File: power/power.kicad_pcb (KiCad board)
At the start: 4 copper layers, 75 x 56 mm, 66 parts, among them J1 GPIO, J10 SCL1, J11 SDA1, J12 SCL2, J13 SDA2, J14 VCC1, J15 GND1, J16 VCC2, J17 GND2, J18 JP_VCC_PWM, J19 Conn_01x01, J2 PWM_OUT, J3 PWM_IN, J4 JP_EXT, J5 JP_VOLTS, J6 I2C_EXT1, J7 I2C_EXT2, J8 PWM_OUT, J9 JP_VCC_PWM, Q1 D15P05, Q2 BC847C, U2 REF5050IDGK, U3 L78L06_SOT89, U5 TPS56A37RPAR

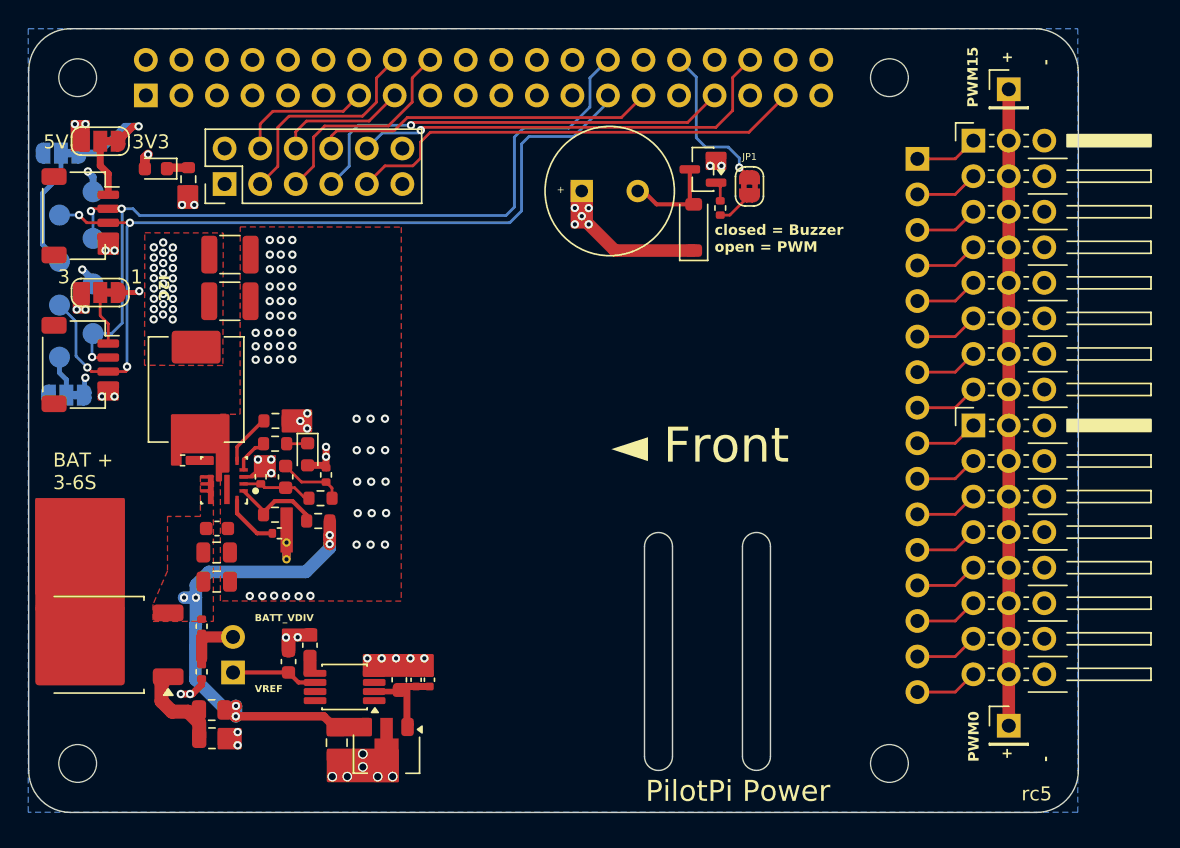
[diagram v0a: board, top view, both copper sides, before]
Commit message: cleanup vias & traces
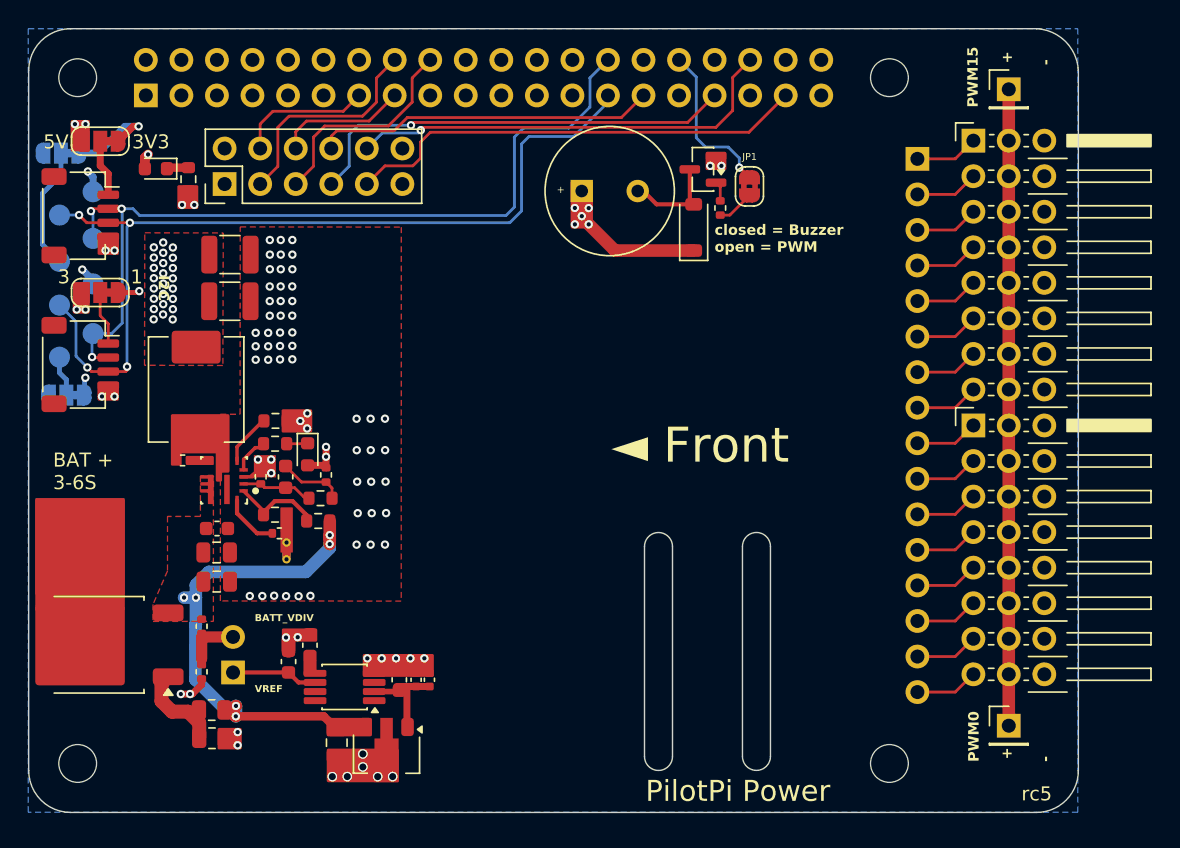
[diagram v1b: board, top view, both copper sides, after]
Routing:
- net +6V: track 7.85 -> 6.99 mm
- net /GPIO0/SDA0: track 65.6 -> 64.8 mm
- net +3V3: track 61.4 -> 60.7 mm
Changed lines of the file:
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@@
 			)
 		)
-		(attr through_hole exclude_from_pos_files dnp)
+		(attr through_hole exclude_from_pos_files)
 		(duplicate_pad_numbers_are_jumpers no)
 		(fp_line
@@
 			)
 		)
-		(attr through_hole exclude_from_pos_files dnp)
+		(attr through_hole exclude_from_pos_files)
 		(duplicate_pad_numbers_are_jumpers no)
 		(fp_line
@@
 			)
 		)
-		(attr through_hole exclude_from_bom dnp)
+		(attr through_hole exclude_from_bom)
 		(duplicate_pad_numbers_are_jumpers no)
 		(fp_line
@@
 			)
 		)
-		(attr through_hole exclude_from_bom dnp)
+		(attr through_hole exclude_from_bom)
 		(duplicate_pad_numbers_are_jumpers no)
 		(fp_line
@@
 			)
 		)
-		(property "Part" "2541WV-2X01P"
+		(property "Part" ""
 			(at 0 0 90)
 			(unlocked yes)
@@
 			)
 		)
-		(attr through_hole exclude_from_pos_files dnp)
+		(attr through_hole exclude_from_pos_files)
 		(duplicate_pad_numbers_are_jumpers no)
 		(fp_line
@@
 			)
 		)
-		(attr through_hole exclude_from_pos_files dnp)
+		(attr through_hole exclude_from_pos_files)
 		(duplicate_pad_numbers_are_jumpers no)
 		(fp_line
@@
 			)
 		)
-		(attr through_hole exclude_from_pos_files dnp)
+		(attr through_hole exclude_from_pos_files)
 		(duplicate_pad_numbers_are_jumpers no)
 		(fp_line
@@
 			)
 		)
-		(attr through_hole exclude_from_pos_files dnp)
+		(attr through_hole exclude_from_pos_files)
 		(duplicate_pad_numbers_are_jumpers no)
 		(fp_line
@@
 	)
 	(segment
-		(start 128.632625 91.000617)
-		(end 128.633153 91.000089)
-		(width 0.5)
-		(layer "F.Cu")
-		(net "+6V")
-	)
-	(segment
 		(start 126.401813 91.000617)
 		(end 126.402056 91.00086)
@@
 	)
 	(segment
-		(start 128.633153 91.000089)
-		(end 128.283153 91.000089)
-		(width 0.5)
-		(layer "F.Cu")
-		(net "+6V")
-	)
-	(segment
 		(start 127.026406 91.00086)
 		(end 127.026406 93.685086)
@@
 	)
 	(segment
-		(start 127.220881 93.740611)
-		(end 127.068469 93.893023)
-		(width 0.5)
-		(layer "F.Cu")
-		(net "+6V")
-	)
-	(segment
 		(start 126.279764 91.000617)
 		(end 126.279764 91.361598)
@@
 	)
 	(segment
-		(start 127.276406 93.685086)
-		(end 127.068469 93.893023)
-		(width 0.5)
-		(layer "F.Cu")
-		(net "+6V")
-	)
-	(segment
 		(start 127.279764 91.000617)
 		(end 128.632625 91.000617)
@@
 	)
 	(segment
-		(start 104.6 62.233333)
-		(end 104.6 61.98)
-		(width 0.5)
-		(layer "B.Cu")
-		(net "GND")
-	)
-	(segment
 		(start 104.6 61.98)
 		(end 103.83 61.21)
@@
 	)
 	(segment
-		(start 104.460176 62.373157)
-		(end 104.6 62.233333)
-		(width 0.5)
-		(layer "B.Cu")
-		(net "GND")
-	)
-	(segment
 		(start 120.461318 90.711598)
 		(end 119.280402 90.711598)
@@
 	)
 	(segment
-		(start 114.60414 89.99586)
-		(end 114.6 90)
-		(width 0.3)
-		(layer "F.Cu")
-		(net "/VREF")
-	)
-	(segment
-		(start 116.779441 78.728828)
-		(end 116.779441 78.561584)
-		(width 0.3)
-		(layer "F.Cu")
-		(net "Net-(U5-EN)")
-	)
-	(segment
 		(start 115.357178 77.033847)
 		(end 116.672159 78.348828)
@@
 	)
 	(segment
-		(start 118.347177 76.788846)
-		(end 118.357178 76.798847)
-		(width 0.2)
-		(layer "F.Cu")
-		(net "Net-(U5-FB)")
-	)
-	(segment
 		(start 116.846732 76.788846)
 		(end 118.347177 76.788846)
@@
 	)
 	(segment
-		(start 116.738413 72.022612)
-		(end 116.807178 72.022612)
-		(width 0.25)
-		(layer "F.Cu")
-		(net "Net-(U5-SS)")
-	)
-	(segment
 		(start 114.887179 73.873846)
 		(end 116.738413 72.022612)
@@
 	)
 	(segment
-		(start 104.53 65.853333)
-		(end 104.6 65.783333)
-		(width 0.2)
-		(layer "B.Cu")
-		(net "/GPIO1{slash}SCL0")
-	)
-	(segment
 		(start 106.64 56.864834)
 		(end 106.68 56.904834)
@@
 	)
 	(segment
-		(start 141.39 49.26)
-		(end 141.39 48.77)
-		(width 0.2)
-		(layer "B.Cu")
-		(net "/GPIO0{slash}SDA0")
-	)
-	(segment
 		(start 103.38 67.392159)
 		(end 103.38 64.93)
@@
 	)
 	(segment
-		(start 107.269888 57.864834)
-		(end 107.35 57.944946)
-		(width 0.2)
-		(layer "B.Cu")
-		(net "/GPIO0{slash}SDA0")
-	)
-	(segment
 		(start 104.191262 68.203421)
 		(end 103.38 67.392159)
@@
 	(segment
 		(start 107.23 57.864834)
-		(end 107.4 57.864834)
-		(width 0.2)
-		(layer "B.Cu")
-		(net "/GPIO0{slash}SDA0")
-	)
-	(segment
-		(start 107.23 57.864834)
 		(end 107.269888 57.864834)
 		(width 0.2)
@@
 	)
 	(segment
-		(start 108.37 48.77)
-		(end 107.855 49.285)
-		(width 0.35)
-		(layer "In1.Cu")
-		(net "+3V3")
-	)
-	(segment
 		(start 107.975 68.655)
 		(end 107.77 68.86)
@@
 	)
 	(segment
-		(start 114.596289 87.463711)
-		(end 114.6 87.46)
-		(width 0.8)
-		(layer "F.Cu")
-		(net "/BATT_VDIV")
-	)
-	(segment
 		(start 112.36 89.038711)
 		(end 112.36 87.463711)
@@
 	)
 	(segment
-		(start 147.24 56.275)
-		(end 147.515 56.55)
-		(width 0.3)
-		(layer "F.Cu")
-		(net "Net-(BZ1--)")
-	)
-	(segment
 		(start 147.515 56.55)
 		(end 144.865 56.55)
@@
 	)
 	(segment
-		(start 119.897178 73.653847)
-		(end 119.927178 73.623847)
-		(width 0.2)
-		(layer "F.Cu")
-		(net "Net-(D1-K)")
-	)
-	(segment
 		(start 150.775 53.93)
 		(end 150.814202 53.93)
@@
 	)
 	(segment
-		(start 150.615 53.77)
-		(end 150.775 53.93)
-		(width 0.2)
-		(layer "B.Cu")
-		(net "/GPIO12{slash}PWM0")
-	)
-	(segment
 		(start 148.37 52.46)
 		(end 149.99 52.46)
@@
 	)
 	(segment
-		(start 109.879548 54.001827)
-		(end 109.951375 53.93)
-		(width 0.6)
-		(layer "F.Cu")
-		(net "Net-(D2-K)")
-	)
-	(segment

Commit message: change package of C16 and C20; add ChatGPT generated logo; use 220nF instead 330nF for C11
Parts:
- C11: value 330nF (334) 10% 50V -> 220nF 10% 50V
- C16, C20: footprint Capacitor_SMD:C_1210_3225Metric -> Capacitor_SMD:C_1206_3216Metric
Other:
- board text added: "Power"
- board text removed: "PilotPi Power"

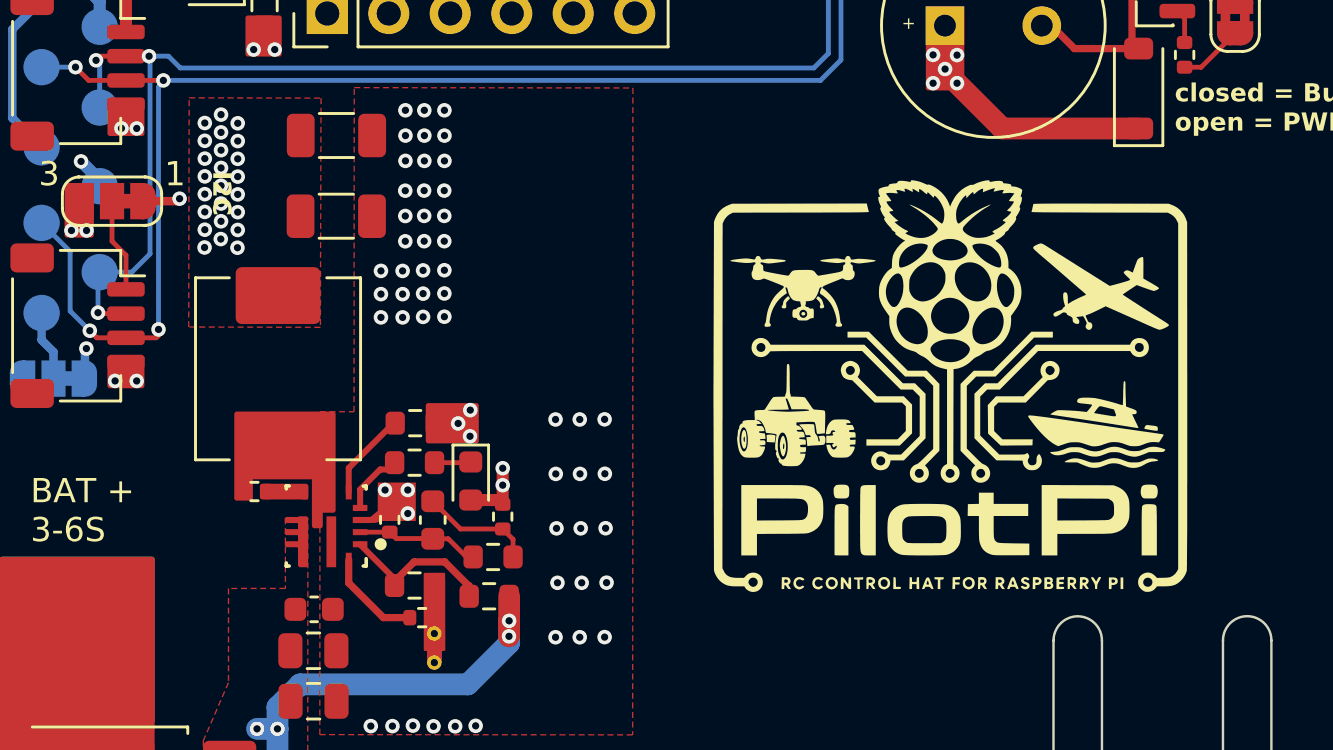
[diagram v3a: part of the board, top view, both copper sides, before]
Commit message: replace inductor
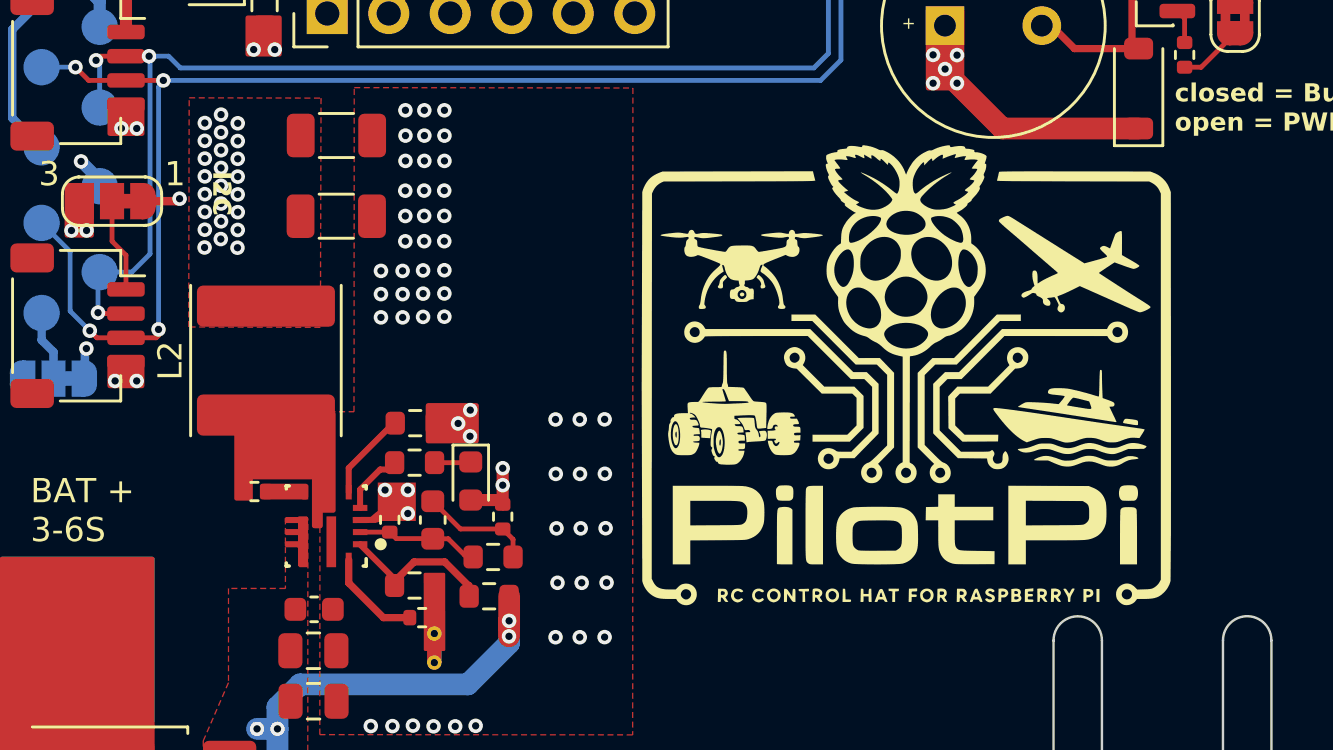
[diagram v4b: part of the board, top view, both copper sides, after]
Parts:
- L2: footprint Inductor_SMD:L_Chilisin_BMRB00060612 -> Inductor_SMD:L_Sunlord_SWPA6045S
- moved L2 0.60 mm to (111.5, 69.4)
